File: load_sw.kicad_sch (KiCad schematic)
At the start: 33 parts, among them Q2 PSMN020-100YS, U14 TPS16851VMAR, U9 LM5050-1

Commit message: Working on 5v supply
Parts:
- renumbered C29 to C20, C23 to C22, C34 to C33, C41 to C40, C46 to C45, C51 to C50, C56 to C55, C61 to C60, D2 to D1, D12 to D11, D17 to D16, D22 to D21, D27 to D26, D7 to D6, NT2 to NT1, NT12 to NT11, NT7 to NT6, Q2 to Q1, R30 to R25, R31 to R26, R32 to R27, R33 to R28, R35 to R34, R40 to R39, R6 to R4, R45 to R44, R50 to R49, R14 to R5, R55 to R54, R60 to R59, R65 to R64, U14 to U13, U9 to U5

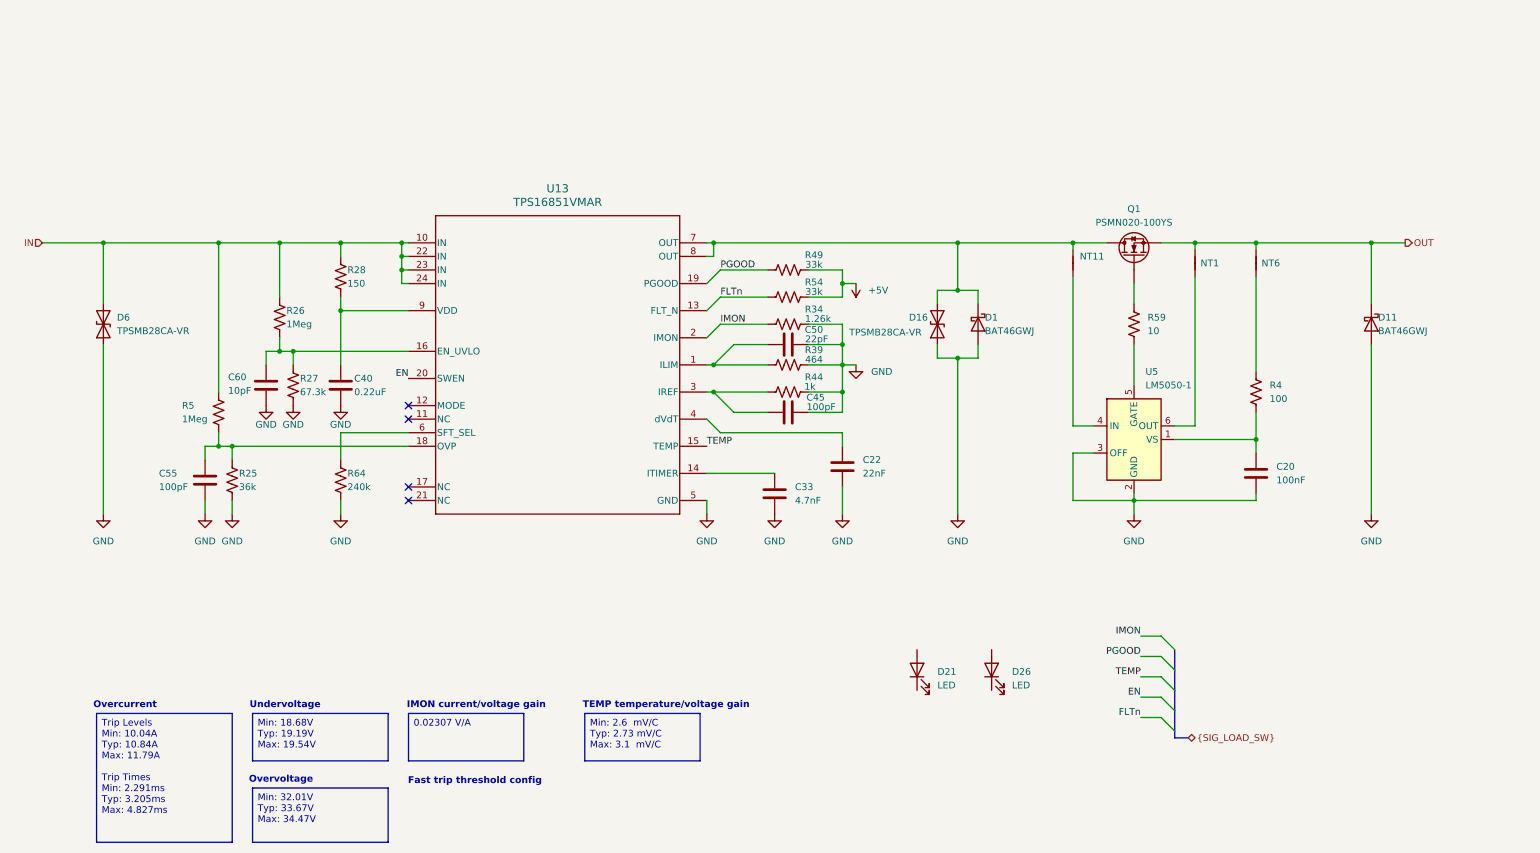
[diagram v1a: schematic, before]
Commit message: Adding in connections to schematic
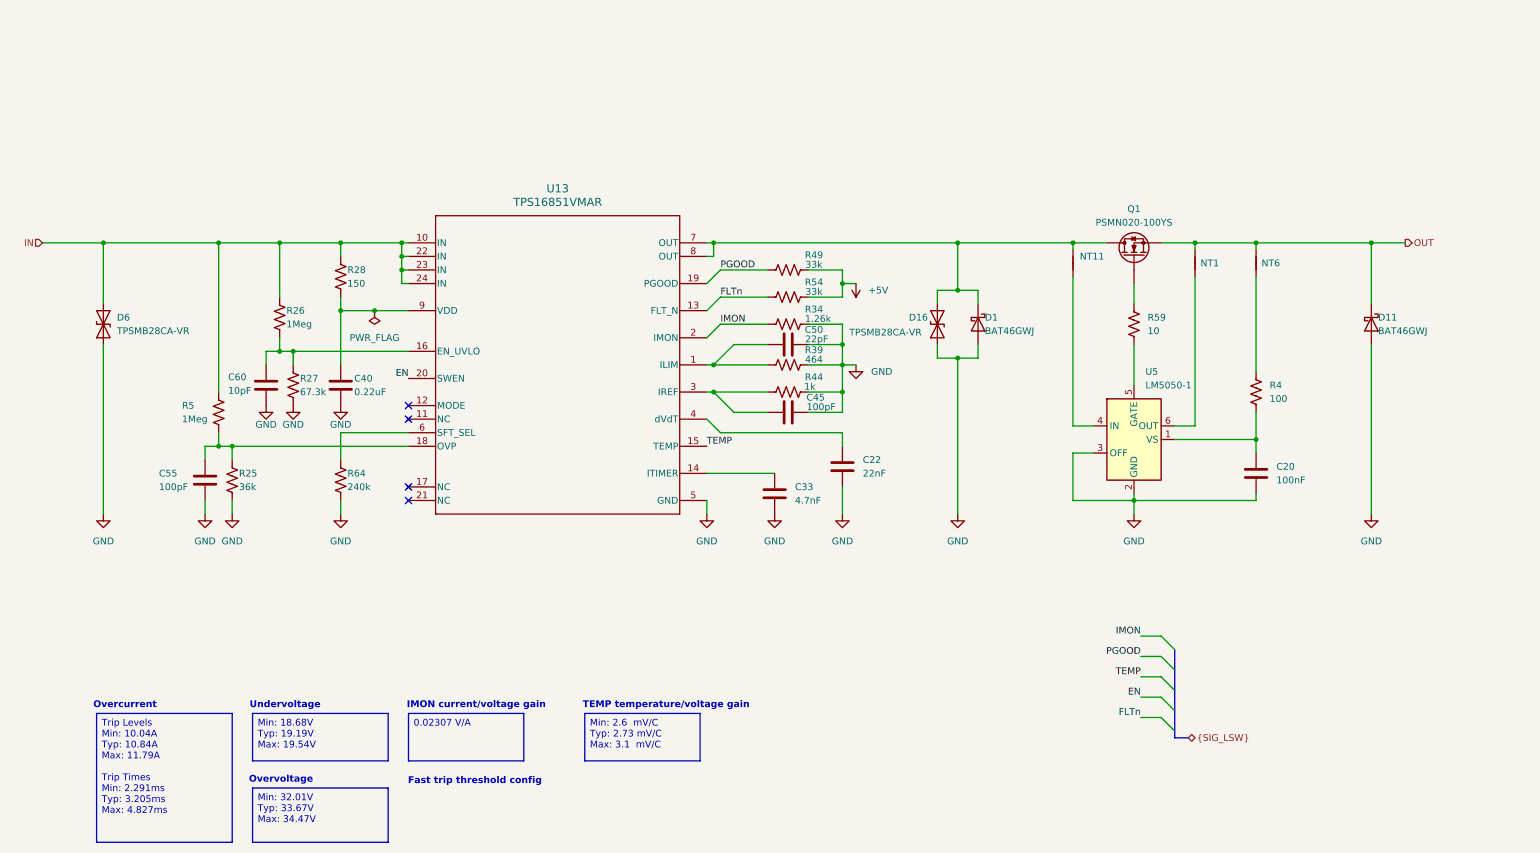
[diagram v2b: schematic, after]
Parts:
- removed D21, D26: LED, symbol Device:LED
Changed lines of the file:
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@@
 		(comment 2 "Reviewer: ")
 	)
-	(bus_alias "SIG_LOAD_SW"
+	(bus_alias "SIG_LSW"
 		(members "IMON" "PGOOD" "TEMP" "EN" "FLTn")
 	)
@@
 	)
 	(junction
+		(at 82.55 76.2)
+		(diameter 0)
+		(color 0 0 0 0)
+	)
+	(junction
 		(at 146.05 63.5)
 		(diameter 0)
@@
 	(wire
 		(pts
+			(xy 82.55 76.2) (xy 88.9 76.2)
+		)
+		(stroke
+			(width 0)
+			(type default)
+		)
+	)
+	(wire
+		(pts
 			(xy 76.2 63.5) (xy 76.2 66.04)
 		)
@@
 	(wire
 		(pts
-			(xy 76.2 76.2) (xy 88.9 76.2)
+			(xy 76.2 76.2) (xy 82.55 76.2)
 		)
 		(stroke
@@
 		)
 	)
-	(hierarchical_label "{SIG_LOAD_SW}"
+	(hierarchical_label "{SIG_LSW}"
 		(shape bidirectional)
 		(at 234.95 156.21 0)
@@
 	)
 	(symbol
-		(lib_id "Device:LED")
-		(at 198.12 143.51 90)
-		(unit 1)
-		(exclude_from_sim no)
-		(in_bom yes)
-		(on_board yes)
-		(dnp no)
-		(fields_autoplaced yes)
-		(property "Reference" "D26"
-			(at 201.93 143.8274 90)
-			(effects
-				(font
-					(size 1.27 1.27)
-				)
-				(justify right)
-			)
-		)
-		(property "Value" "LED"
-			(at 201.93 146.3674 90)
-			(effects
-				(font
-					(size 1.27 1.27)
-				)
-				(justify right)
-			)
-		)
-		(property "Footprint" ""
-			(at 198.12 143.51 0)
-			(effects
-				(font
-					(size 1.27 1.27)
-				)
-				(hide yes)
-			)
-		)
-		(property "Datasheet" "~"
-			(at 198.12 143.51 0)
-			(effects
-				(font
-					(size 1.27 1.27)
-				)
-				(hide yes)
-			)
-		)
-		(property "Description" "Light emitting diode"
-			(at 198.12 143.51 0)
-			(effects
-				(font
-					(size 1.27 1.27)
-				)
-				(hide yes)
-			)
-		)
-		(property "Sim.Pins" "1=K 2=A"
-			(at 198.12 143.51 0)
-			(effects
-				(font
-					(size 1.27 1.27)
-				)
-				(hide yes)
-			)
-		)
-		(pin "1"
-		)
-		(pin "2"
-		)
-		(instances
-			(project "PowerBoard"
-				(path "/99785679-20de-4827-b4cc-bc3c187068c9/9564929a-642e-4163-88c2-45054b63a5ed/5ab37dee-300b-447e-9b13-e5d50b13d849"
-					(reference "D26")
-					(unit 1)
-				)
-				(path "/99785679-20de-4827-b4cc-bc3c187068c9/9564929a-642e-4163-88c2-45054b63a5ed/70687909-9f63-4b18-b374-bb5d5688a7a1"
-					(reference "D30")
-					(unit 1)
-				)
-				(path "/99785679-20de-4827-b4cc-bc3c187068c9/9564929a-642e-4163-88c2-45054b63a5ed/aa92e4e1-fc74-44a9-8187-6c9770b466cf"
-					(reference "D29")
-					(unit 1)
-				)
-				(path "/99785679-20de-4827-b4cc-bc3c187068c9/9564929a-642e-4163-88c2-45054b63a5ed/b9213479-bc9a-4fd6-a1a6-404b21448f58"
-					(reference "D27")
-					(unit 1)
-				)
-				(path "/99785679-20de-4827-b4cc-bc3c187068c9/9564929a-642e-4163-88c2-45054b63a5ed/f2327609-10a0-4227-bf59-7648982e83ec"
-					(reference "D28")
-					(unit 1)
-				)
-			)
-		)
-	)
-	(symbol
 		(lib_id "Device:C")
 		(at 62.23 90.17 0)
@@
 	)
 	(symbol
-		(lib_id "Device:LED")
-		(at 184.15 143.51 90)
+		(lib_id "power:PWR_FLAG")
+		(at 82.55 76.2 180)
 		(unit 1)
 		(exclude_from_sim no)
@@
 		(dnp no)
 		(fields_autoplaced yes)
-		(property "Reference" "D21"
-			(at 187.96 143.8274 90)
+		(property "Reference" "#FLG02"
+			(at 82.55 78.105 0)
 			(effects
 				(font
 					(size 1.27 1.27)
 				)
-				(justify right)
+				(hide yes)
 			)
 		)
-		(property "Value" "LED"
-			(at 187.96 146.3674 90)
+		(property "Value" "PWR_FLAG"
+			(at 82.55 81.28 0)
 			(effects
 				(font
 					(size 1.27 1.27)
 				)
-				(justify right)
 			)
 		)
 		(property "Footprint" ""
-			(at 184.15 143.51 0)
+			(at 82.55 76.2 0)
 			(effects
 				(font
@@
 		)
 		(property "Datasheet" "~"
-			(at 184.15 143.51 0)
-			(effects
-				(font
-					(size 1.27 1.27)
-				)
-				(hide yes)
-			)
-		)
-		(property "Description" "Light emitting diode"
-			(at 184.15 143.51 0)
+			(at 82.55 76.2 0)
 			(effects
 				(font
@@
 			)
 		)
-		(property "Sim.Pins" "1=K 2=A"
-			(at 184.15 143.51 0)
+		(property "Description" "Special symbol for telling ERC where power comes from"
+			(at 82.55 76.2 0)
 			(effects
 				(font
@@
 		(pin "1"
 		)
-		(pin "2"
-		)
 		(instances
-			(project "PowerBoard"
+			(project ""
 				(path "/99785679-20de-4827-b4cc-bc3c187068c9/9564929a-642e-4163-88c2-45054b63a5ed/5ab37dee-300b-447e-9b13-e5d50b13d849"
-					(reference "D21")
+					(reference "#FLG02")
 					(unit 1)
 				)
 				(path "/99785679-20de-4827-b4cc-bc3c187068c9/9564929a-642e-4163-88c2-45054b63a5ed/70687909-9f63-4b18-b374-bb5d5688a7a1"
-					(reference "D25")
+					(reference "#FLG06")
 					(unit 1)
 				)
 				(path "/99785679-20de-4827-b4cc-bc3c187068c9/9564929a-642e-4163-88c2-45054b63a5ed/aa92e4e1-fc74-44a9-8187-6c9770b466cf"
-					(reference "D24")
+					(reference "#FLG05")
 					(unit 1)
 				)
 				(path "/99785679-20de-4827-b4cc-bc3c187068c9/9564929a-642e-4163-88c2-45054b63a5ed/b9213479-bc9a-4fd6-a1a6-404b21448f58"
-					(reference "D22")
+					(reference "#FLG03")
 					(unit 1)
 				)
 				(path "/99785679-20de-4827-b4cc-bc3c187068c9/9564929a-642e-4163-88c2-45054b63a5ed/f2327609-10a0-4227-bf59-7648982e83ec"
-					(reference "D23")
+					(reference "#FLG04")
 					(unit 1)
 				)

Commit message: Working on layout now
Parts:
- U4: renamed from U13; footprint VMA0023A-MFG -> _Power_Board:05-08-7040_ADI
- renumbered C55 to C20, C60 to C21, C40 to C22, C33 to C23, C50 to C24, C45 to C25, C22 to C26, C20 to C27, D6 to D1, D16 to D2, D1 to D3, D11 to D4, NT11 to NT1, NT1 to NT2, NT6 to NT3, R26 to R10, R27 to R11, R28 to R12, R64 to R13, R49 to R14, R54 to R15, R34 to R16, R39 to R17, R44 to R18, R59 to R19, R4 to R20, R5 to R8, R25 to R9

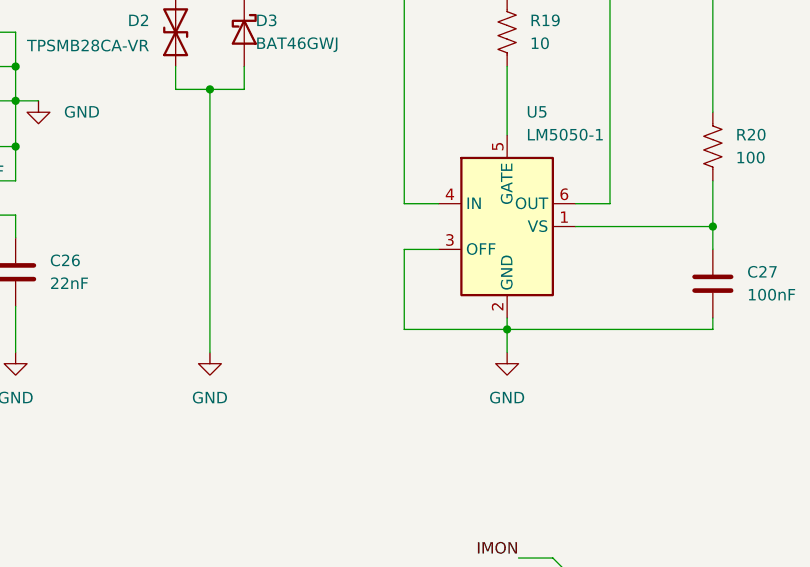
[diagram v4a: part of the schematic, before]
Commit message: PowerBoard update with LVBUS
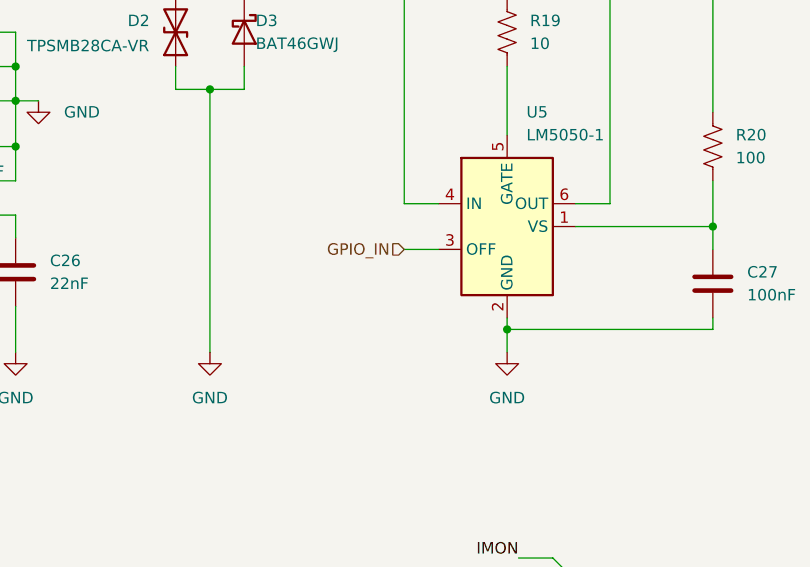
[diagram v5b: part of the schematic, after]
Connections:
- net GND: no longer U5.3 (OFF)
- new net GPIO_IN: U5.3 (OFF)

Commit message: Cleaning up schematic
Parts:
- C79: renamed from C22; Mfr KEMET -> YAGEO; Mfr P/N C0603C221F5GACAUTO -> CC0603JRX7R9BB224; Supplier_1 Digikey -> (none); Supplier_1 P/N 399-C0603C221F5GACAUTOTR-ND -> (none); Supplier_1 Unit Price 0.85000 -> (none); Supplier_2 (none) -> JLCPCB; Supplier_2 P/N (none) -> C519575; Supplier_2 Price @ Qty (none) -> 1; Supplier_2 Unit Price (none) -> 0.0140
- C86: renamed from C23; Mfr P/N GCM1885C2A471FA16D -> GCM1885C1H472FA16D; Supplier_1 Digikey -> (none); Supplier_1 P/N 490-GCM1885C2A471FA16DTR-ND -> (none); Supplier_1 Price @ Qty 1 -> (none); Supplier_1 Unit Price 0.16000 -> (none); Supplier_2 (none) -> JLCPCB; Supplier_2 P/N (none) -> C883564; Supplier_2 Price @ Qty (none) -> 1; Supplier_2 Unit Price (none) -> 0.0707
- D10: renamed from D2; now not fitted
- D11: renamed from D3; now not fitted
- renumbered C20 to C77, C21 to C78, C24 to C87, C25 to C88, C26 to C89, C27 to C90, D4 to D15, D1 to D9, NT1 to NT7, NT2 to NT8, NT3 to NT9, Q1 to Q3, R8 to R51, R9 to R52, R10 to R53, R11 to R55, R12 to R56, R13 to R57, R14 to R58, R15 to R59, R16 to R60, R17 to R61, R18 to R62, R19 to R63, R20 to R64, U4 to U15, U5 to U16
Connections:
- net GPIO_IN renamed EN_DIODE
